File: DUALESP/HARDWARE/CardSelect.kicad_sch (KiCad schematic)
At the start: 13 parts, among them SW1 IO PORT ADDR, U1 74LS244, U10 74HC595, U11 74HC165, U17 74LS08, U2 74LS245, U3 74LS244, U4 74LS04, U6 74LS07, U7 74LS32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

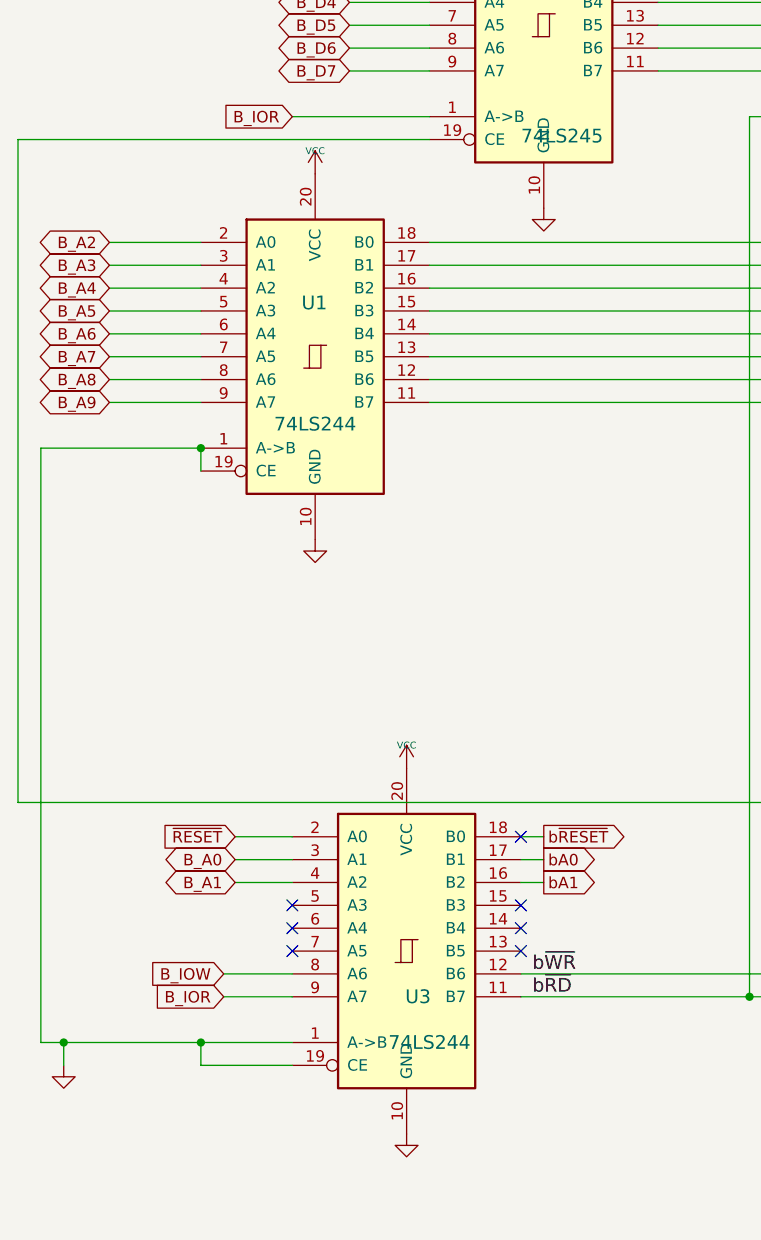
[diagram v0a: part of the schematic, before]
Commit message: fix ESP layout issues
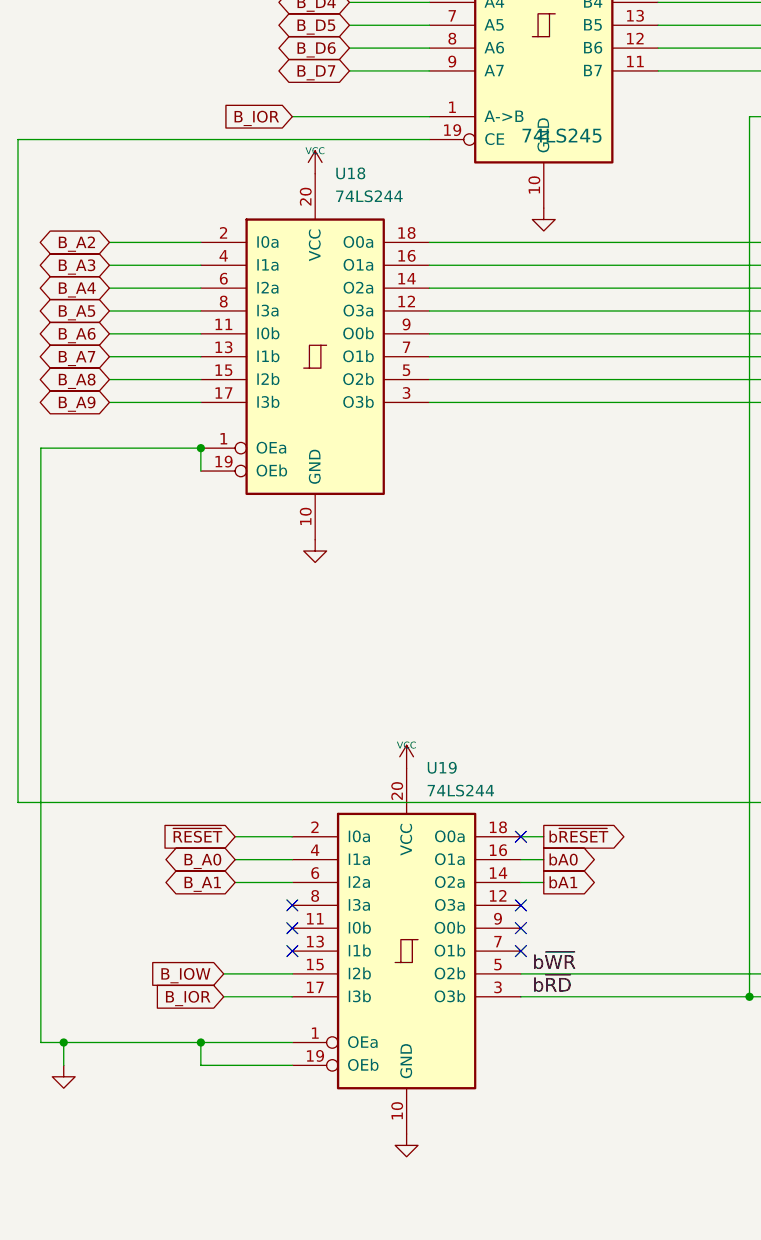
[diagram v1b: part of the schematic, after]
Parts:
- removed U1, U3: 74LS244, Custom:STD_DDW_DIP20, symbol 74xx:74LS245
- added U18, U19: 74LS244, Custom:STD_DDW_DIP20, symbol 74xx:74LS244
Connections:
- net B_A0: now also U19.4 (I1a)
- net B_A1: now also U19.6 (I2a)
- net B_A2: now also U18.2 (I0a)
- net B_A3: now also U18.4 (I1a)
- net B_A4: now also U18.6 (I2a)
- net B_A5: now also U18.8 (I3a)
- net B_A6: now also U18.11 (I0b)
- net B_A7: now also U18.13 (I1b)
- net B_A8: now also U18.15 (I2b)
- net B_A9: now also U18.17 (I3b)
- net B_IOR: now also U19.17 (I3b)
- net B_IOW: now also U19.15 (I2b)
- net GND: now also U18.1 (OEa), U18.10 (GND), U18.19 (OEb), U19.1 (OEa), U19.10 (GND), U19.19 (OEb)
- net VCC: now also U18.20 (VCC), U19.20 (VCC)
- net bA0: now also U19.16 (O1a)
- net bA1: now also U19.14 (O2a)
- net b~{RD}: now also U19.3 (O3b)
- net b~{RESET}: now also U19.18 (O0a)
- net b~{WR}: now also U19.5 (O2b)
- net ~{RESET}: now also U19.2 (I0a)
- net at U9.11 (P4): now also U18.9 (O0b)
- net at U9.13 (P5): now also U18.7 (O1b)
- net at U9.15 (P6): now also U18.5 (O2b)
- net at U9.17 (P7): now also U18.3 (O3b)
- net at U9.2 (P0): now also U18.18 (O0a)
- net at U9.4 (P1): now also U18.16 (O1a)
- net at U9.6 (P2): now also U18.14 (O2a)
- net at U9.8 (P3): now also U18.12 (O3a)
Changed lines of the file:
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@@
 	(title_block
 		(title "ISA DUAL ESP32")
-		(date "2025-06-14")
-		(rev "V1")
+		(date "2025-06-21")
+		(rev "V1.1")
 	)
 	(junction
@@
 	)
 	(junction
+		(at 53.34 91.44)
+		(diameter 0)
+		(color 0 0 0 0)
+	)
+	(junction
 		(at 127 96.52)
 		(diameter 0)
@@
 	)
 	(junction
-		(at 53.34 91.44)
-		(diameter 0)
-		(color 0 0 0 0)
-	)
-	(junction
 		(at 127 101.6)
 		(diameter 0)
@@
 	)
 	(symbol
+		(lib_id "74xx:74LS244")
+		(at 66.04 81.28 0)
+		(unit 1)
+		(exclude_from_sim no)
+		(in_bom yes)
+		(on_board yes)
+		(dnp no)
+		(fields_autoplaced yes)
+		(property "Reference" "U18"
+			(at 68.2341 60.96 0)
+			(effects
+				(font
+					(size 1.27 1.27)
+				)
+				(justify left)
+			)
+		)
+		(property "Value" "74LS244"
+			(at 68.2341 63.5 0)
+			(effects
+				(font
+					(size 1.27 1.27)
+				)
+				(justify left)
+			)
+		)
+		(property "Footprint" "Custom:STD_DDW_DIP20"
+			(at 66.04 81.28 0)
+			(effects
+				(font
+					(size 1.27 1.27)
+				)
+				(hide yes)
+			)
+		)
+		(property "Datasheet" "http://www.ti.com/lit/ds/symlink/sn74ls244.pdf"
+			(at 66.04 81.28 0)
+			(effects
+				(font
+					(size 1.27 1.27)
+				)
+				(hide yes)
+			)
+		)
+		(property "Description" "Octal Buffer and Line Driver With 3-State Output, active-low enables, non-inverting outputs"
+			(at 66.04 81.28 0)
+			(effects
+				(font
+					(size 1.27 1.27)
+				)
+				(hide yes)
+			)
+		)
+		(pin "16"
+		)
+		(pin "10"
+		)
+		(pin "11"
+		)
+		(pin "19"
+		)
+		(pin "15"
+		)
+		(pin "14"
+		)
+		(pin "2"
+		)
+		(pin "3"
+		)
+		(pin "6"
+		)
+		(pin "12"
+		)
+		(pin "13"
+		)
+		(pin "4"
+		)
+		(pin "17"
+		)
+		(pin "20"
+		)
+		(pin "1"
+		)
+		(pin "18"
+		)
+		(pin "5"
+		)
+		(pin "9"
+		)
+		(pin "7"
+		)
+		(pin "8"
+		)
+		(instances
+			(project ""
+				(path "/1489d9c1-97ed-41d1-bf7e-e97aaaa797c2/bb50d935-6cee-4c02-9854-42100f2ef4fd"
+					(reference "U18")
+					(unit 1)
+				)
+			)
+		)
+	)
+	(symbol
 		(lib_id "power:VCC")
 		(at 165.1 114.3 0)
@@
 	)
 	(symbol
+		(lib_id "74xx:74LS244")
+		(at 76.2 147.32 0)
+		(unit 1)
+		(exclude_from_sim no)
+		(in_bom yes)
+		(on_board yes)
+		(dnp no)
+		(fields_autoplaced yes)
+		(property "Reference" "U19"
+			(at 78.3941 127 0)
+			(effects
+				(font
+					(size 1.27 1.27)
+				)
+				(justify left)
+			)
+		)
+		(property "Value" "74LS244"
+			(at 78.3941 129.54 0)
+			(effects
+				(font
+					(size 1.27 1.27)
+				)
+				(justify left)
+			)
+		)
+		(property "Footprint" "Custom:STD_DDW_DIP20"
+			(at 76.2 147.32 0)
+			(effects
+				(font
+					(size 1.27 1.27)
+				)
+				(hide yes)
+			)
+		)
+		(property "Datasheet" "http://www.ti.com/lit/ds/symlink/sn74ls244.pdf"
+			(at 76.2 147.32 0)
+			(effects
+				(font
+					(size 1.27 1.27)
+				)
+				(hide yes)
+			)
+		)
+		(property "Description" "Octal Buffer and Line Driver With 3-State Output, active-low enables, non-inverting outputs"
+			(at 76.2 147.32 0)
+			(effects
+				(font
+					(size 1.27 1.27)
+				)
+				(hide yes)
+			)
+		)
+		(pin "13"
+		)
+		(pin "10"
+		)
+		(pin "7"
+		)
+		(pin "20"
+		)
+		(pin "15"
+		)
+		(pin "8"
+		)
+		(pin "11"
+		)
+		(pin "9"
+		)
+		(pin "12"
+		)
+		(pin "14"
+		)
+		(pin "19"
+		)
+		(pin "2"
+		)
+		(pin "18"
+		)
+		(pin "6"
+		)
+		(pin "16"
+		)
+		(pin "3"
+		)
+		(pin "4"
+		)
+		(pin "17"
+		)
+		(pin "5"
+		)
+		(pin "1"
+		)
+		(instances
+			(project ""
+				(path "/1489d9c1-97ed-41d1-bf7e-e97aaaa797c2/bb50d935-6cee-4c02-9854-42100f2ef4fd"
+					(reference "U19")
+					(unit 1)
+				)
+			)
+		)
+	)
+	(symbol
 		(lib_id "74xx:74LS07")
 		(at 275.59 191.77 0)
@@
 					(unit 1)
 				)
-			)
-		)
-	)
-	(symbol
-		(lib_id "74xx:74LS245")
-		(at 66.04 81.28 0)
-		(unit 1)
-		(exclude_from_sim no)
-		(in_bom yes)
-		(on_board yes)
-		(dnp no)
-		(property "Reference" "U1"
-			(at 64.516 76.2 0)
-			(effects
-				(font
-					(size 1.524 1.524)
-				)
-				(justify left bottom)
-			)
-		)
-		(property "Value" "74LS244"
-			(at 61.468 87.884 0)
-			(effects
-				(font
-					(size 1.524 1.524)
-				)
-				(justify left top)
-			)
-		)
-		(property "Footprint" "Custom:STD_DDW_DIP20"
-			(at 66.04 81.28 0)
-			(effects
-				(font
-					(size 1.27 1.27)
-				)
-				(hide yes)
-			)
-		)
-		(property "Datasheet" "http://www.ti.com/lit/gpn/sn74LS245"
-			(at 66.04 81.28 0)
-			(effects
-				(font
-					(size 1.27 1.27)
-				)
-				(hide yes)
-			)
-		)
-		(property "Description" "Octal BUS Transceivers, 3-State outputs"
-			(at 66.04 81.28 0)
-			(effects
-				(font
-					(size 1.27 1.27)
-				)
-				(hide yes)
-			)
-		)
-		(pin "10"
-		)
-		(pin "20"
-		)
-		(pin "1"
-		)
-		(pin "11"
-		)
-		(pin "12"
-		)
-		(pin "13"
-		)
-		(pin "14"
-		)
-		(pin "15"
-		)
-		(pin "16"
-		)
-		(pin "17"
-		)
-		(pin "18"
-		)
-		(pin "19"
-		)
-		(pin "2"
-		)
-		(pin "3"
-		)
-		(pin "4"
-		)
-		(pin "5"
-		)
-		(pin "6"
-		)
-		(pin "7"
-		)
-		(pin "8"
-		)
-		(pin "9"
-		)
-		(instances
-			(project "DUALESP"
-				(path "/1489d9c1-97ed-41d1-bf7e-e97aaaa797c2/bb50d935-6cee-4c02-9854-42100f2ef4fd"
-					(reference "U1")
-					(unit 1)
-				)
-			)
-		)
-	)
-	(symbol
-		(lib_id "74xx:74LS245")
-		(at 76.2 147.32 0)
-		(unit 1)
-		(exclude_from_sim no)
-		(in_bom yes)
-		(on_board yes)
-		(dnp no)
-		(property "Reference" "U3"
-			(at 77.47 152.4 0)
-			(effects
-				(font
-					(size 1.524 1.524)
-				)
-			)
-		)
-		(property "Value" "74LS244"
-			(at 78.74 157.48 0)
-			(effects
-				(font
-					(size 1.524 1.524)
-				)
-			)
-		)
-		(property "Footprint" "Custom:STD_DDW_DIP20"
-			(at 76.2 147.32 0)
-			(effects
-				(font
-					(size 1.27 1.27)
-				)
-				(hide yes)
-			)
-		)
-		(property "Datasheet" "http://www.ti.com/lit/gpn/sn74LS245"
-			(at 76.2 147.32 0)
-			(effects
-				(font
-					(size 1.27 1.27)
-				)
-				(hide yes)
-			)
-		)
-		(property "Description" "Octal BUS Transceivers, 3-State outputs"
-			(at 76.2 147.32 0)
-			(effects
-				(font
-					(size 1.27 1.27)
-				)
-				(hide yes)
-			)
-		)
-		(pin "10"
-		)
-		(pin "20"
-		)
-		(pin "1"
-		)
-		(pin "11"
-		)
-		(pin "12"
-		)
-		(pin "13"
-		)
-		(pin "14"
-		)
-		(pin "15"
-		)
-		(pin "16"
-		)
-		(pin "17"
-		)
-		(pin "18"
-		)
-		(pin "19"
-		)
-		(pin "2"
-		)
-		(pin "3"
-		)
-		(pin "4"
-		)
-		(pin "5"
-		)
-		(pin "6"
-		)
-		(pin "7"
-		)
-		(pin "8"
-		)
-		(pin "9"
-		)
-		(instances
-			(project "DUALESP"
-				(path "/1489d9c1-97ed-41d1-bf7e-e97aaaa797c2/bb50d935-6cee-4c02-9854-42100f2ef4fd"
-					(reference "U3")
-					(unit 1)
-				)

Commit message: ESPIO updates
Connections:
- net bD0: now reaches U10.15 (QA), U11.11 (D0), U2.18 (B0)
- net bD1: now reaches U10.1 (QB), U11.12 (D1), U2.17 (B1)
- net bD2: now reaches U10.2 (QC), U11.13 (D2), U2.16 (B2)
- net bD3: now reaches U10.3 (QD), U11.14 (D3), U2.15 (B3)
- net bD4: now reaches U10.4 (QE), U11.3 (D4), U2.14 (B4)
- net bD5: now reaches U10.5 (QF), U11.4 (D5), U2.13 (B5)
- net bD6: now reaches U10.6 (QG), U11.5 (D6), U2.12 (B6)
- net bD7: now reaches U10.7 (QH), U11.6 (D7), U2.11 (B7)

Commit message: ESPIO updates
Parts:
- removed unit 1 of U6
- removed unit 2 of U6
- removed unit 4 of U6
- removed unit 3 of U6
- U11: value 74HC165 -> 74ACT165
- U19: value 74LS244 -> 74ALS244
- U7, U8: value 74LS32 -> 74F32
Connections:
- net ~{ESP0_RD}: now also U8.8
- net ~{ESP0_WR}: now also U8.6
- net ~{ESP1_RD}: now also U8.11
- net ~{ESP1_WR}: now also U8.3
